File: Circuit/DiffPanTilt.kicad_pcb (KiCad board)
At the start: 2 copper layers, 48.3 x 48.3 mm, 18 parts, among them J1 Power, J2 Stepper 1, J3 Stepper 2, J4 BT, J5 Stepper 1 Power, J6 Stepper 2 Power, J7 12V Input, J8 5V Output, J9 Display, SW1 Switch

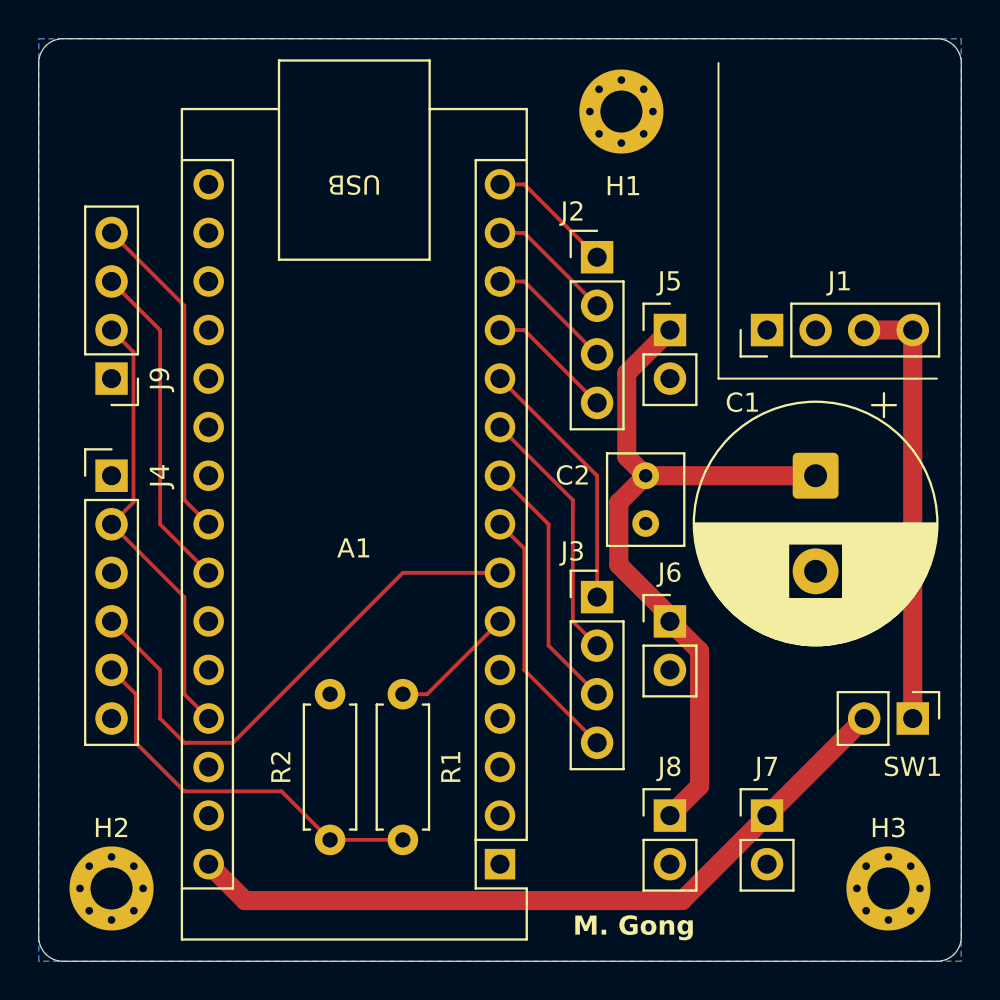
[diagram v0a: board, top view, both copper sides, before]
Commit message: [Circuit] Change the footprint of J1 to pin socket, and fine tune the PCB layout
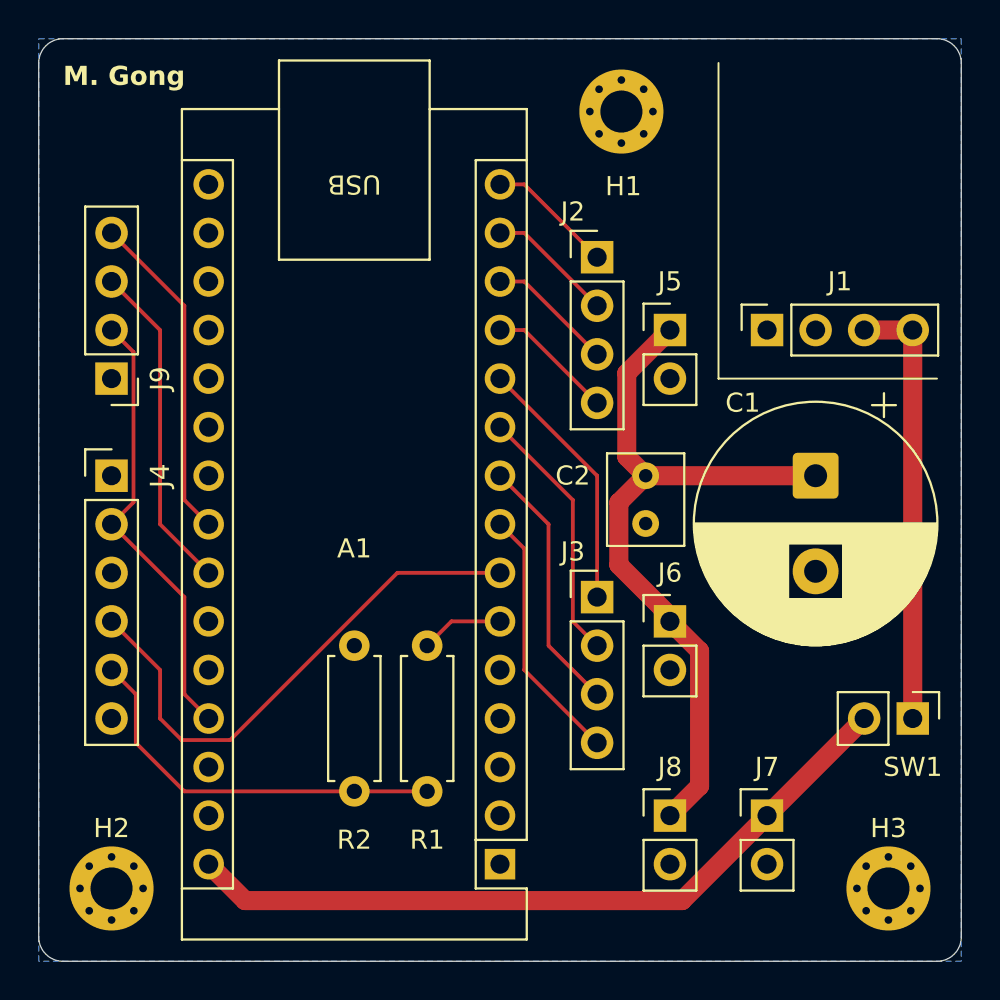
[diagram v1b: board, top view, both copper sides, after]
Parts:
- J1: footprint Connector_PinHeader_2.54mm:PinHeader_1x04_P2.54mm_Vertical -> Connector_PinSocket_2.54mm:PinSocket_1x04_P2.54mm_Vertical
- moved R2 2.84 mm to (118.1, 92.7)
- moved R1 2.84 mm to (121.9, 85.1)
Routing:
- net Net-(A1-D3): track 6.66 -> 4.34 mm
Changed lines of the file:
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@@
 	(footprint "Resistor_THT:R_Axial_DIN0207_L6.3mm_D2.5mm_P7.62mm_Horizontal"
 		(layer "F.Cu")
-		(at 120.65 87.63 -90)
+		(at 121.92 85.09 -90)
 		(descr "Resistor, Axial_DIN0207 series, Axial, Horizontal, pin pitch=7.62mm, 0.25W = 1/4W, length*diameter=6.3*2.5mm^2, http://cdn-reichelt.de/documents/datenblatt/B400/1_4W%23YAG.pdf")
 		(tags "Resistor Axial_DIN0207 series Axial Horizontal pin pitch 7.62mm 0.25W = 1/4W length 6.3mm diameter 2.5mm")
 		(property "Reference" "R1"
-			(at 3.81 -2.54 90)
+			(at 10.16 0 180)
 			(layer "F.SilkS")
 			(effects
@@
 	(footprint "Resistor_THT:R_Axial_DIN0207_L6.3mm_D2.5mm_P7.62mm_Horizontal"
 		(layer "F.Cu")
-		(at 116.84 95.25 90)
+		(at 118.11 92.71 90)
 		(descr "Resistor, Axial_DIN0207 series, Axial, Horizontal, pin pitch=7.62mm, 0.25W = 1/4W, length*diameter=6.3*2.5mm^2, http://cdn-reichelt.de/documents/datenblatt/B400/1_4W%23YAG.pdf")
 		(tags "Resistor Axial_DIN0207 series Axial Horizontal pin pitch 7.62mm 0.25W = 1/4W length 6.3mm diameter 2.5mm")
 		(property "Reference" "R2"
-			(at 3.81 -2.54 90)
+			(at -2.54 0 180)
 			(layer "F.SilkS")
 			(effects
@@
 		(embedded_fonts no)
 	)
-	(footprint "Connector_PinHeader_2.54mm:PinHeader_1x04_P2.54mm_Vertical"
+	(footprint "Connector_PinSocket_2.54mm:PinSocket_1x04_P2.54mm_Vertical"
 		(layer "F.Cu")
 		(at 139.7 68.58 90)
-		(descr "Through hole straight pin header, 1x04, 2.54mm pitch, single row")
-		(tags "Through hole pin header THT 1x04 2.54mm single row")
+		(descr "Through hole straight socket strip, 1x04, 2.54mm pitch, single row (from Kicad 4.0.7), script generated")
+		(tags "Through hole socket strip THT 1x04 2.54mm single row")
 		(property "Reference" "J1"
 			(at 2.54 3.81 180)
@@
 		)
 		(property "Value" "Power"
-			(at 0 10 90)
+			(at 2.54 3.81 180)
 			(layer "F.Fab")
 			(effects
@@
 		(attr through_hole)
 		(fp_line
-			(start -1.38 -1.38)
-			(end 0 -1.38)
+			(start 1.33 -1.33)
+			(end 1.33 0)
 			(stroke
 				(width 0.12)
@@
 		)
 		(fp_line
-			(start -1.38 0)
-			(end -1.38 -1.38)
+			(start 0 -1.33)
+			(end 1.33 -1.33)
 			(stroke
 				(width 0.12)
@@
 		)
 		(fp_line
-			(start 1.38 1.27)
-			(end 1.38 9)
+			(start 1.33 1.27)
+			(end 1.33 8.95)
 			(stroke
 				(width 0.12)
@@
 		)
 		(fp_line
-			(start -1.38 1.27)
-			(end 1.38 1.27)
+			(start -1.33 1.27)
+			(end 1.33 1.27)
 			(stroke
 				(width 0.12)
@@
 		)
 		(fp_line
-			(start -1.38 1.27)
-			(end -1.38 9)
+			(start -1.33 1.27)
+			(end -1.33 8.95)
 			(stroke
 				(width 0.12)
@@
 		)
 		(fp_line
-			(start -1.38 9)
-			(end 1.38 9)
+			(start -1.33 8.95)
+			(end 1.33 8.95)
 			(stroke
 				(width 0.12)
@@
 		)
 		(fp_line
-			(start 1.77 -1.77)
-			(end -1.77 -1.77)
+			(start 1.75 -1.8)
+			(end 1.75 9.4)
 			(stroke
 				(width 0.05)
@@
 		)
 		(fp_line
-			(start -1.77 -1.77)
-			(end -1.77 9.39)
+			(start -1.8 -1.8)
+			(end 1.75 -1.8)
 			(stroke
 				(width 0.05)
@@
 		)
 		(fp_line
-			(start 1.77 9.39)
-			(end 1.77 -1.77)
+			(start 1.75 9.4)
+			(end -1.8 9.4)
 			(stroke
 				(width 0.05)
@@
 		)
 		(fp_line
-			(start -1.77 9.39)
-			(end 1.77 9.39)
+			(start -1.8 9.4)
+			(end -1.8 -1.8)
 			(stroke
 				(width 0.05)
@@
 		)
 		(fp_line
-			(start 1.27 -1.27)
-			(end 1.27 8.89)
+			(start 0.635 -1.27)
+			(end 1.27 -0.635)
 			(stroke
 				(width 0.1)
@@
 		)
 		(fp_line
-			(start -0.635 -1.27)
-			(end 1.27 -1.27)
+			(start -1.27 -1.27)
+			(end 0.635 -1.27)
 			(stroke
 				(width 0.1)
@@
 		)
 		(fp_line
-			(start -1.27 -0.635)
-			(end -0.635 -1.27)
+			(start 1.27 -0.635)
+			(end 1.27 8.89)
 			(stroke
 				(width 0.1)
@@
 		(fp_line
 			(start -1.27 8.89)
-			(end -1.27 -0.635)
+			(end -1.27 -1.27)
 			(stroke
 				(width 0.1)
@@
 		)
 		(fp_text user "${REFERENCE}"
-			(at 0 3.81 0)
+			(at 0 3.81 180)
 			(layer "F.Fab")
 			(effects
@@
 		)
 		(embedded_fonts no)
-		(model "${KICAD9_3DMODEL_DIR}/Connector_PinHeader_2.54mm.3dshapes/PinHeader_1x04_P2.54mm_Vertical.step"
+		(model "${KICAD9_3DMODEL_DIR}/Connector_PinSocket_2.54mm.3dshapes/PinSocket_1x04_P2.54mm_Vertical.step"
 			(offset
 				(xyz 0 0 0)
@@
 	)
 	(gr_text "M. Gong"
-		(at 129.54 100.33 0)
+		(at 102.87 55.88 0)
 		(layer "F.SilkS")
 		(effects
@@
 	)
 	(segment
-		(start 109.22 90.17)
-		(end 107.95 88.9)
+		(start 125.73 81.28)
+		(end 120.36295 81.28)
 		(width 0.2)
 		(layer "F.Cu")
@@
 	)
 	(segment
-		(start 125.73 81.28)
-		(end 120.65 81.28)
+		(start 107.95 86.36)
+		(end 105.41 83.82)
 		(width 0.2)
 		(layer "F.Cu")
@@
 	)
 	(segment
-		(start 107.95 88.9)
-		(end 107.95 86.36)
+		(start 120.36295 81.28)
+		(end 111.616476 90.026474)
 		(width 0.2)
 		(layer "F.Cu")
@@
 	)
 	(segment
-		(start 107.95 86.36)
-		(end 105.41 83.82)
+		(start 109.076474 90.026474)
+		(end 107.95 88.9)
 		(width 0.2)
 		(layer "F.Cu")
@@
 	)
 	(segment
-		(start 120.65 81.28)
-		(end 111.76 90.17)
+		(start 107.95 88.9)
+		(end 107.95 86.36)
 		(width 0.2)
 		(layer "F.Cu")
@@
 	)
 	(segment
-		(start 111.76 90.17)
-		(end 109.22 90.17)
+		(start 111.616476 90.026474)
+		(end 109.076474 90.026474)
 		(width 0.2)
 		(layer "F.Cu")
@@
 	)
 	(segment
-		(start 121.92 87.63)
-		(end 125.73 83.82)
+		(start 121.92 85.09)
+		(end 123.19 83.82)
 		(width 0.2)
 		(layer "F.Cu")
@@
 	)
 	(segment
-		(start 120.65 87.63)
-		(end 121.92 87.63)
+		(start 125.73 83.82)
+		(end 123.19 83.82)
 		(width 0.2)
 		(layer "F.Cu")
@@
 	)
 	(segment
-		(start 116.84 95.25)
-		(end 120.65 95.25)
-		(width 0.2)
-		(layer "F.Cu")
-		(net 33)
-	)
-	(segment
-		(start 106.68 87.63)
-		(end 106.68 90.17)
+		(start 118.11 92.71)
+		(end 121.92 92.71)
 		(width 0.2)
 		(layer "F.Cu")
@@
 	)
 	(segment
-		(start 109.22 92.71)
-		(end 114.3 92.71)
+		(start 106.68 87.63)
+		(end 106.68 90.17)
 		(width 0.2)
 		(layer "F.Cu")
@@
 	)
 	(segment
-		(start 114.3 92.71)
-		(end 116.84 95.25)
+		(start 109.22 92.71)
+		(end 118.11 92.71)
 		(width 0.2)
 		(layer "F.Cu")
